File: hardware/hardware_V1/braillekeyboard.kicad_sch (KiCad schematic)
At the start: 43 parts, among them J1 Conn_01x15_Socket, J2 Conn_01x15_Socket, J3 Barrel_Jack_Switch, M1 Motor_DC, M2 Motor_DC, M3 Motor_DC, M4 Motor_DC, M5 Motor_DC, M6 Motor_DC, Q1 BC337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

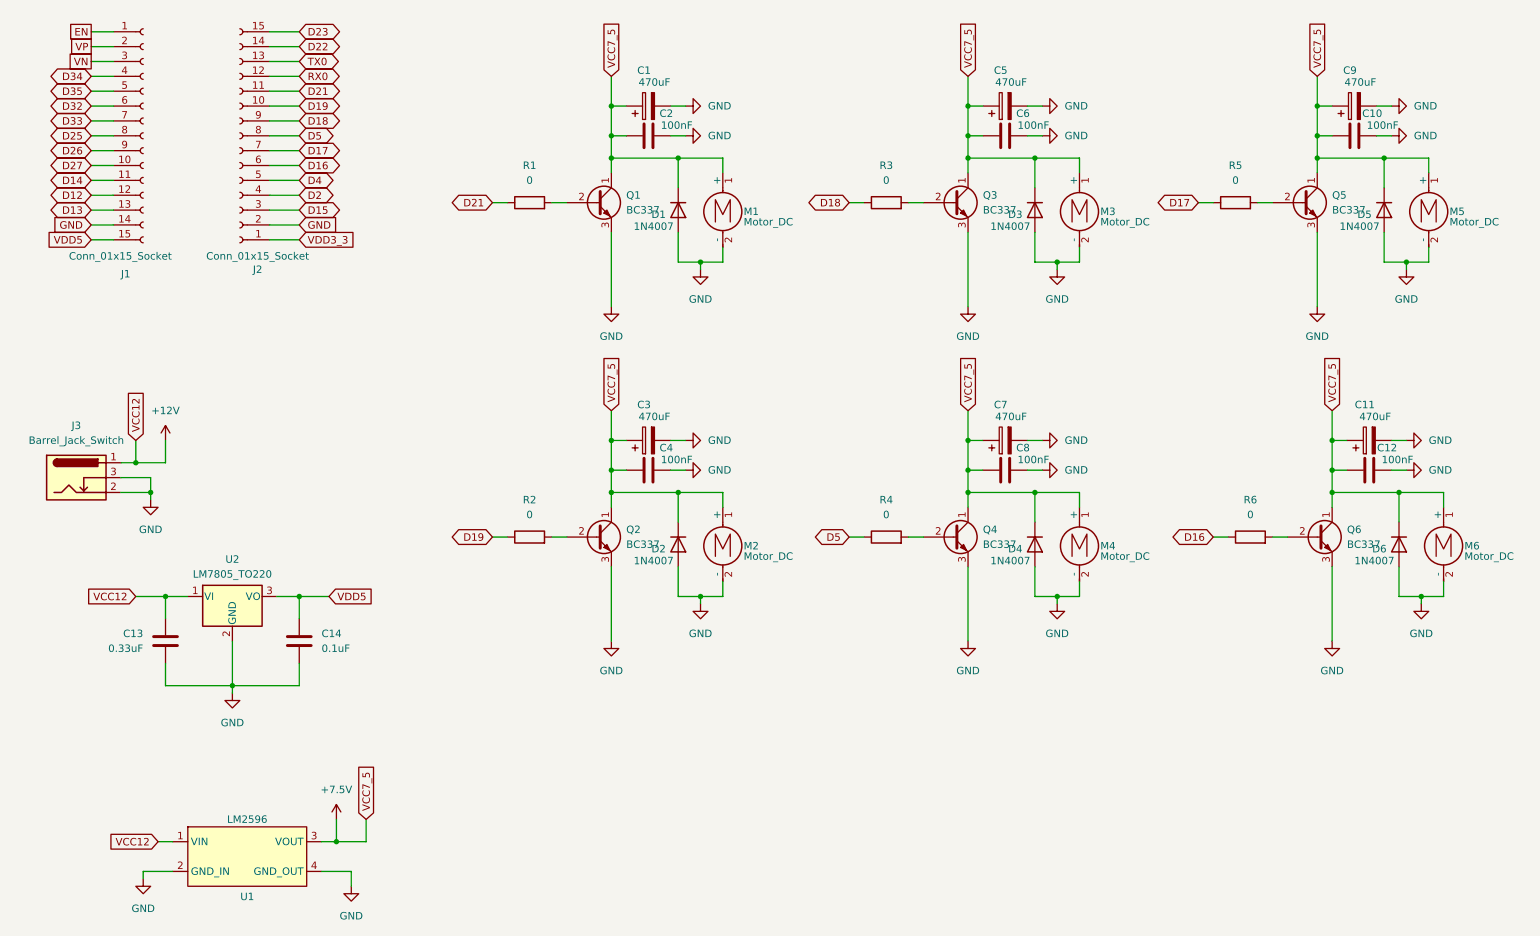
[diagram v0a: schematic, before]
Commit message: Inclusão do latch no circuito, ampliação para 36 motores
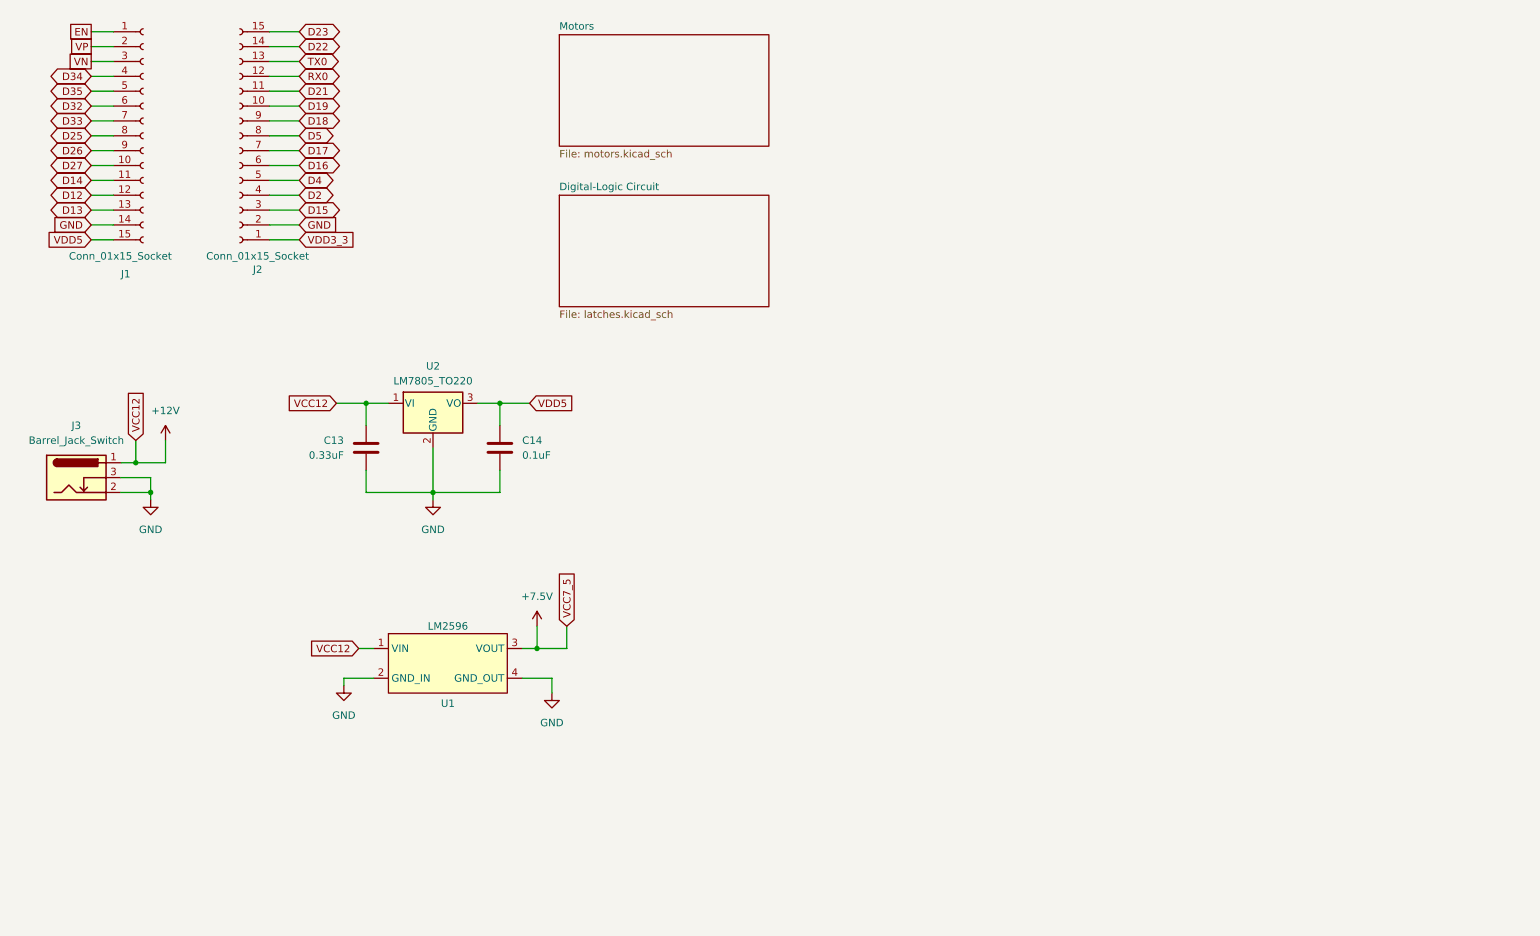
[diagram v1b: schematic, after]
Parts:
- removed C1, C11, C3, C5, C7, C9: 470uF, 470u:CAPPRD500W60D1050H1750, symbol Device:C_Polarized
- removed C10, C12, C2, C4, C6, C8: 100nF, 100u:615R100GAD10, symbol Device:C
- removed D1, D2, D3, D4, D5, D6: 1N4007, Diode_THT:D_DO-41_SOD81_P10.16mm_Horizontal, symbol Diode:1N4007
- removed M1, M2, M3, M4, M5, M6: Motor_DC, Connector_JST:JST_XH_B2B-XH-AM_1x02_P2.50mm_Vertical, symbol Motor:Motor_DC
- removed Q1, Q2, Q3, Q4, Q5, Q6: BC337, bc337:BC33716TA, symbol Transistor_BJT:BC337
- removed R1, R2, R3, R4, R5, R6: 0, Resistor_THT:R_Axial_DIN0617_L17.0mm_D6.0mm_P25.40mm_Horizontal, symbol Device:R
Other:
- added sheet Digital-Logic Circuit (latches.kicad_sch)
- added sheet Motors (motors.kicad_sch)
- moved on the sheet: C13, C14, U1, U2
